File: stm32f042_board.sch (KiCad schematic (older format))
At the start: 23 parts, among them J1 Conn_01x12_Female, J2 Conn_01x12_Female, J3 USB_B_Micro, J5 JTAG/SWD, U1 STM32F042F6Px, U2 MCP1802, U3 USBLC6-2SC6

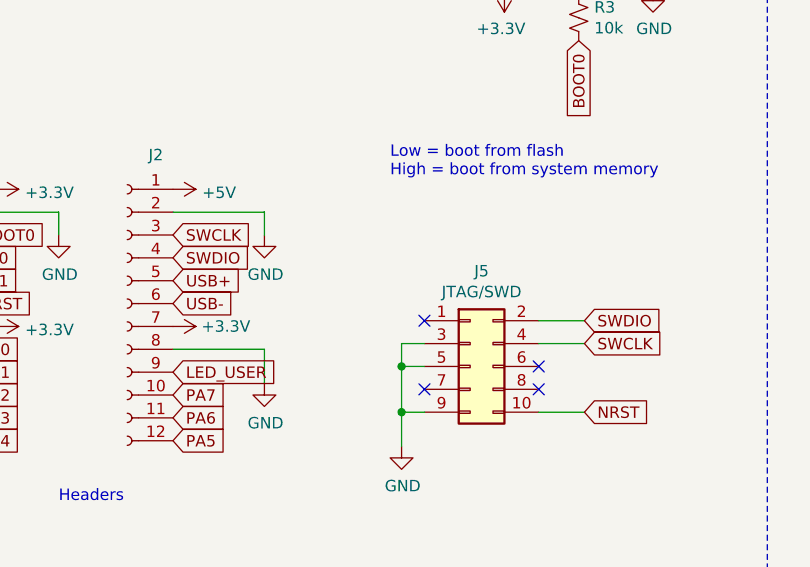
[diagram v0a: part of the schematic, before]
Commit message: oops. connect 3v3 on jtag header.
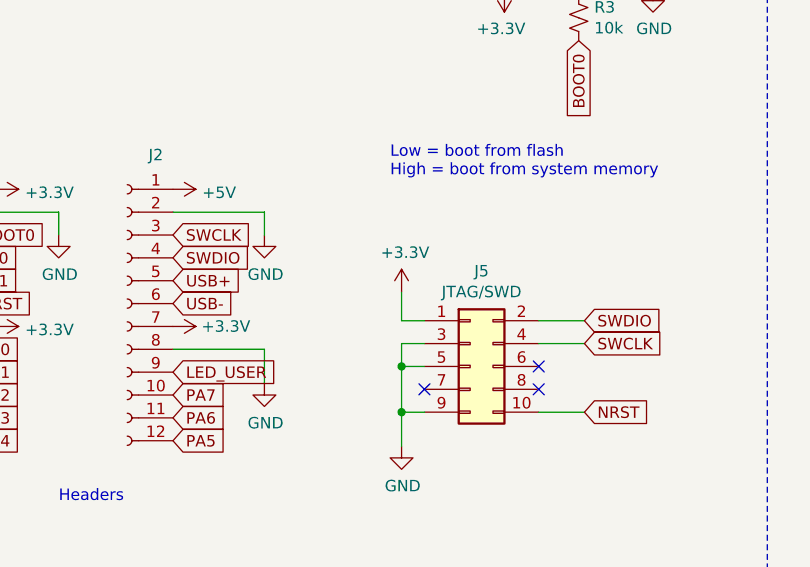
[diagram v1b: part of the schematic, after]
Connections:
- net +3V3: now also J5.1 (Pin_1)
- no-connect marks 5 -> 4
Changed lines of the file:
@@
 	1    0    0    -1
 $EndComp
-NoConn ~ 4775 4175
 NoConn ~ 5275 4375
 NoConn ~ 5275 4475
@@
 Wire Wire Line
 	5100 1325 5100 1425
+$Comp
+L power:+3.3V #PWR?
+U 1 1 60535E20
+P 4675 4050
+F 0 "#PWR?" H 4675 3900 50  0001 C CNN
+F 1 "+3.3V" H 4690 4223 50  0000 C CNN
+F 2 "" H 4675 4050 50  0001 C CNN
+F 3 "" H 4675 4050 50  0001 C CNN
+	1    4675 4050
+	1    0    0    -1
+$EndComp
+Wire Wire Line
+	4675 4050 4675 4175
+Wire Wire Line
+	4675 4175 4775 4175
 $EndSCHEMATC
